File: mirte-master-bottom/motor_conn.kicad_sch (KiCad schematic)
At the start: 7 parts, among them U6 PCA9685PW

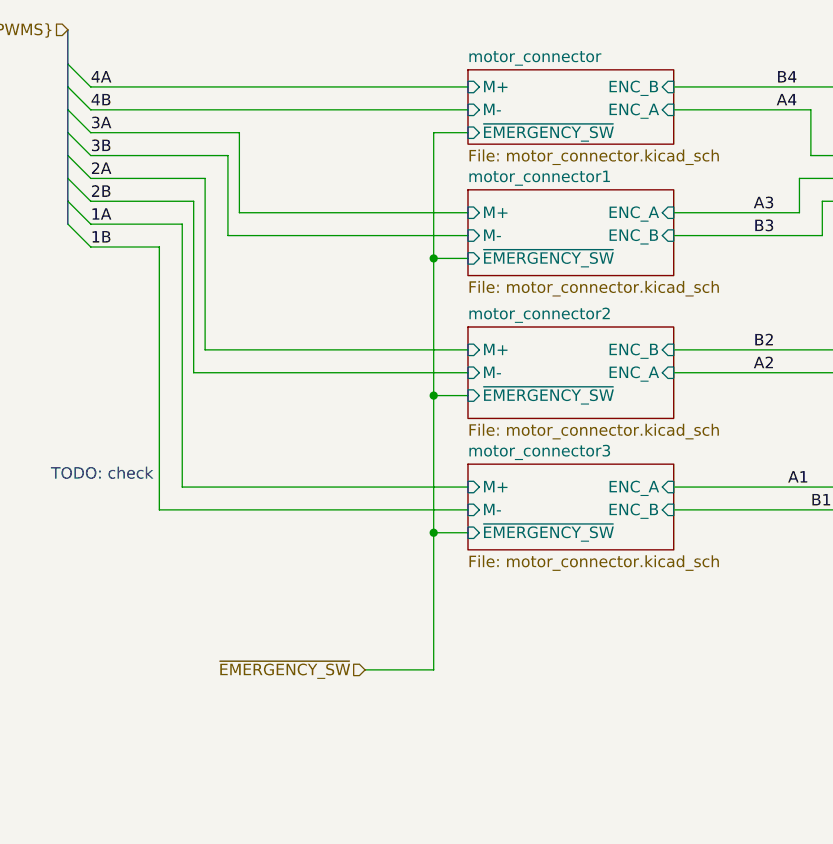
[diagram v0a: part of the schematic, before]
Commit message: Cleanups, text fixes for 3rd test pcb with assembly
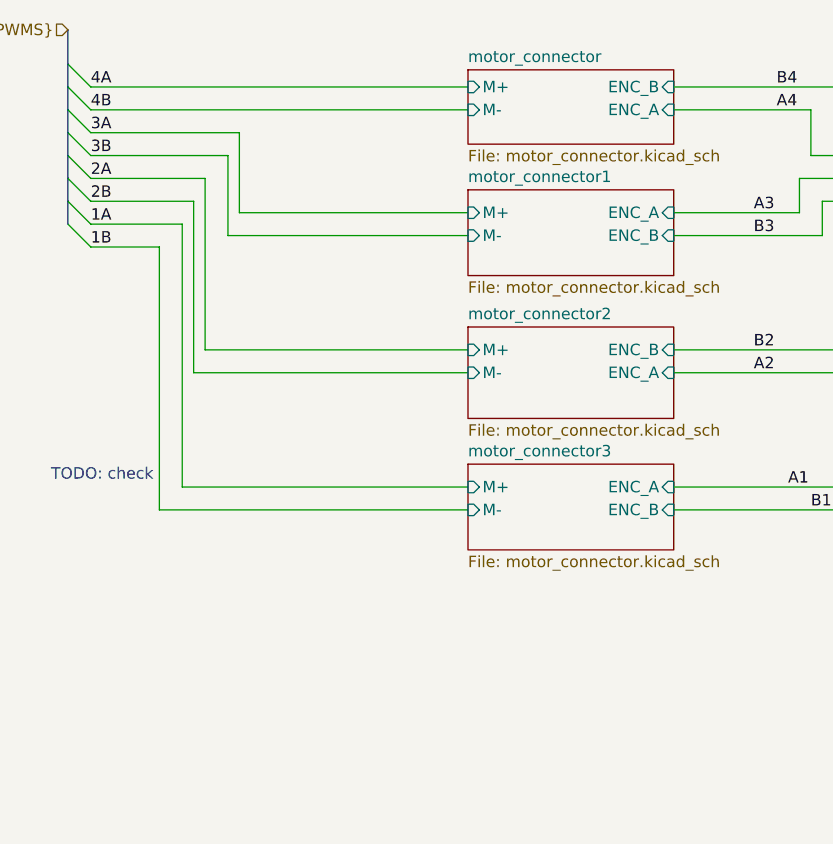
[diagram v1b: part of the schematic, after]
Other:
- sheet motor_connector ports: added none; removed ~{EMERGENCY_SW}
- sheet motor_connector1 ports: added none; removed ~{EMERGENCY_SW}
- sheet motor_connector2 ports: added none; removed ~{EMERGENCY_SW}
- sheet motor_connector3 ports: added none; removed ~{EMERGENCY_SW}
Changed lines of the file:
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@@
-	)
-	(junction
-		(at 149.86 105.41)
-		(diameter 0)
-		(color 0 0 0 0)
-	)
-	(junction
-		(at 149.86 90.17)
-		(diameter 0)
-		(color 0 0 0 0)
 	)
 	(junction
@@
 	)
 	(junction
-		(at 149.86 74.93)
-		(diameter 0)
-		(color 0 0 0 0)
-	)
-	(junction
 		(at 50.8 161.29)
 		(diameter 0)
@@
 	(wire
 		(pts
-			(xy 149.86 105.41) (xy 149.86 120.65)
-		)
-		(stroke
-			(width 0)
-			(type default)
-			(color 255 0 0 1)
-		)
-	)
-	(wire
-		(pts
 			(xy 111.76 60.96) (xy 128.27 60.96)
 		)
@@
 	(wire
 		(pts
-			(xy 149.86 60.96) (xy 149.86 74.93)
-		)
-		(stroke
-			(width 0)
-			(type default)
-			(color 255 0 0 1)
-		)
-	)
-	(wire
-		(pts
 			(xy 176.53 58.42) (xy 191.77 58.42)
 		)
@@
 	(wire
 		(pts
-			(xy 149.86 105.41) (xy 153.67 105.41)
-		)
-		(stroke
-			(width 0)
-			(type default)
-			(color 255 0 0 1)
-		)
-	)
-	(wire
-		(pts
 			(xy 196.85 60.96) (xy 208.28 60.96)
 		)
@@
 		)
 	)
-	(wire
-		(pts
-			(xy 142.24 120.65) (xy 149.86 120.65)
-		)
-		(stroke
-			(width 0)
-			(type default)
-			(color 255 0 0 1)
-		)
-	)
 	(bus
 		(pts
@@
 	(wire
 		(pts
-			(xy 149.86 74.93) (xy 149.86 90.17)
-		)
-		(stroke
-			(width 0)
-			(type default)
-			(color 255 0 0 1)
-		)
-	)
-	(wire
-		(pts
 			(xy 208.28 78.74) (xy 201.93 78.74)
 		)
@@
 	(wire
 		(pts
-			(xy 149.86 90.17) (xy 149.86 105.41)
-		)
-		(stroke
-			(width 0)
-			(type default)
-			(color 255 0 0 1)
-		)
-	)
-	(wire
-		(pts
-			(xy 149.86 90.17) (xy 153.67 90.17)
-		)
-		(stroke
-			(width 0)
-			(type default)
-			(color 255 0 0 1)
-		)
-	)
-	(wire
-		(pts
 			(xy 48.26 161.29) (xy 50.8 161.29)
 		)
@@
 	(wire
 		(pts
-			(xy 153.67 60.96) (xy 149.86 60.96)
-		)
-		(stroke
-			(width 0)
-			(type default)
-			(color 255 0 0 1)
-		)
-	)
-	(wire
-		(pts
 			(xy 194.31 85.09) (xy 194.31 71.12)
 		)
@@
 			(width 0)
 			(type default)
-		)
-	)
-	(wire
-		(pts
-			(xy 149.86 74.93) (xy 153.67 74.93)
-		)
-		(stroke
-			(width 0)
-			(type default)
-			(color 255 0 0 1)
 		)
 	)
@@
 		(shape input)
 		(at 109.22 49.53 180)
-		(effects
-			(font
-				(size 1.27 1.27)
-			)
-			(justify right)
-		)
-	)
-	(hierarchical_label "~{EMERGENCY_SW}"
-		(shape input)
-		(at 142.24 120.65 180)
 		(effects
 			(font
@@
 			)
 		)
-		(pin "~{EMERGENCY_SW}" input
-			(at 153.67 105.41 180)
-			(effects
-				(font
-					(size 1.27 1.27)
-				)
-				(justify left)
-			)
-		)
 		(instances
 			(project "mirte-master"
@@
 			)
 		)
-		(pin "~{EMERGENCY_SW}" input
-			(at 153.67 60.96 180)
-			(effects
-				(font
-					(size 1.27 1.27)
-				)
-				(justify left)
-			)
-		)
 		(instances
 			(project "mirte-master"
@@
 			)
 		)
-		(pin "~{EMERGENCY_SW}" input
-			(at 153.67 74.93 180)
-			(effects
-				(font
-					(size 1.27 1.27)
-				)
-				(justify left)
-			)
-		)
 		(instances
 			(project "mirte-master"
@@
 			)
 		)
-		(pin "~{EMERGENCY_SW}" input
-			(at 153.67 90.17 180)
-			(effects
-				(font
-					(size 1.27 1.27)
-				)
-				(justify left)
-			)
-		)

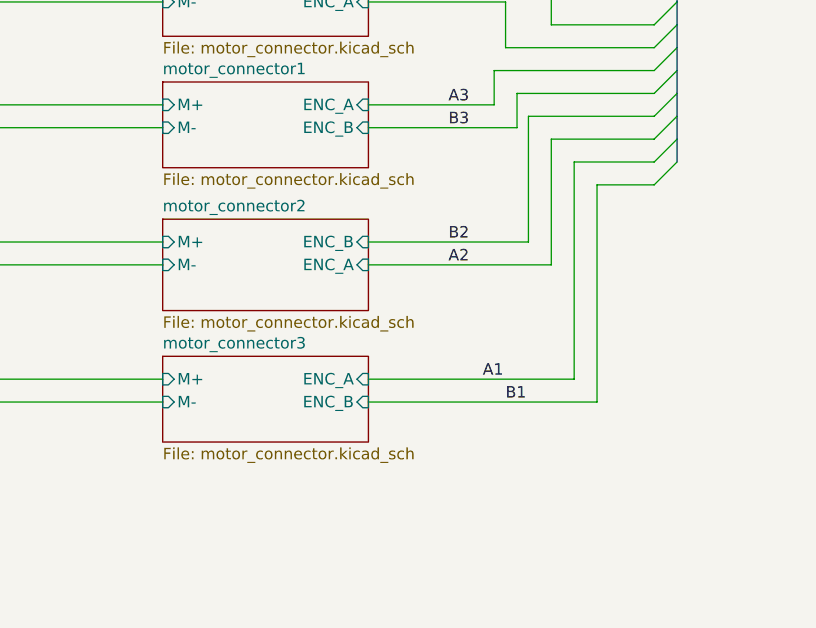
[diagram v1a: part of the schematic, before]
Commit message: MM: motor leds same color, emergency button screw, start button led screw, drc exclusions
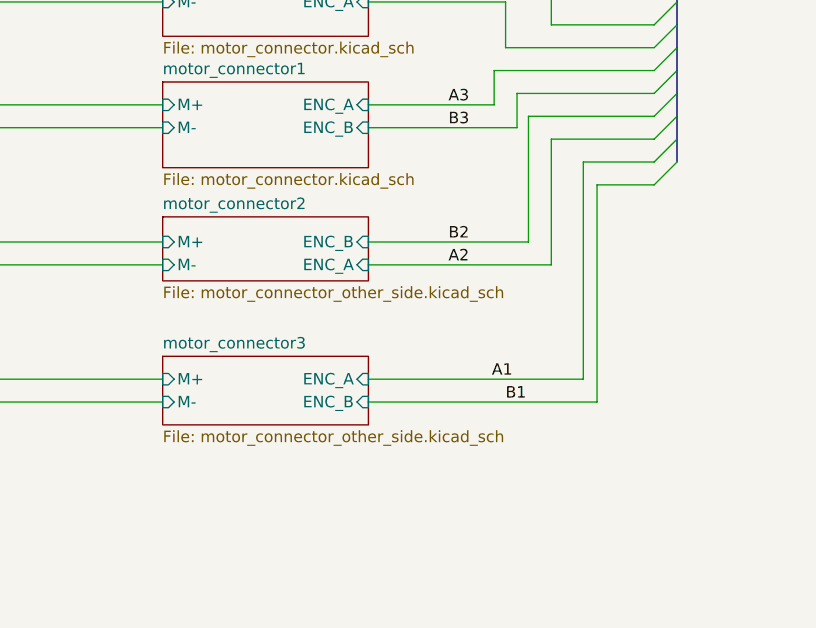
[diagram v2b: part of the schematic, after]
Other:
- sheet motor_connector2: file motor_connector.kicad_sch -> motor_connector_other_side.kicad_sch
- sheet motor_connector3: file motor_connector.kicad_sch -> motor_connector_other_side.kicad_sch
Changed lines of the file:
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@@
+	(wire
+		(pts
+			(xy 176.53 102.87) (xy 201.93 102.87)
+		)
+		(stroke
+			(width 0)
+			(type default)
+		)
+	)
 	(wire
 		(pts
@@
 	(wire
 		(pts
-			(xy 199.39 76.2) (xy 208.28 76.2)
+			(xy 200.406 76.2) (xy 208.28 76.2)
 		)
 		(stroke
@@
 	(wire
 		(pts
-			(xy 176.53 100.33) (xy 199.39 100.33)
+			(xy 176.53 100.33) (xy 200.406 100.33)
 		)
 		(stroke
@@
 	(wire
 		(pts
-			(xy 199.39 100.33) (xy 199.39 76.2)
+			(xy 200.406 100.33) (xy 200.406 76.2)
 		)
 		(stroke
@@
 		(pts
 			(xy 190.5 69.85) (xy 190.5 66.04)
-		)
-		(stroke
-			(width 0)
-			(type default)
-		)
-	)
-	(wire
-		(pts
-			(xy 201.93 102.87) (xy 176.53 102.87)
 		)
 		(stroke
@@
 	)
 	(label "A1"
-		(at 189.23 100.33 0)
+		(at 190.246 100.33 0)
 		(effects
 			(font
@@
 	(sheet
 		(at 153.67 97.79)
-		(size 22.86 9.525)
+		(size 22.86 7.62)
 		(exclude_from_sim no)
 		(in_bom yes)
@@
 			)
 		)
-		(property "Sheetfile" "motor_connector.kicad_sch"
-			(at 153.67 107.8996 0)
+		(property "Sheetfile" "motor_connector_other_side.kicad_sch"
+			(at 153.67 105.9946 0)
 			(effects
 				(font
@@
 	)
 	(sheet
-		(at 153.67 82.55)
-		(size 22.86 10.16)
+		(at 153.67 82.296)
+		(size 22.86 7.112)
 		(exclude_from_sim no)
 		(in_bom yes)
@@
 		)
 		(property "Sheetname" "motor_connector2"
-			(at 153.67 81.8384 0)
+			(at 153.67 81.5844 0)
 			(effects
 				(font
@@
 			)
 		)
-		(property "Sheetfile" "motor_connector.kicad_sch"
-			(at 153.67 93.2946 0)
-			(effects
-				(font
+		(property "Sheetfile" "motor_connector_other_side.kicad_sch"
+			(at 153.67 89.9926 0)
+			(effects
+				(font

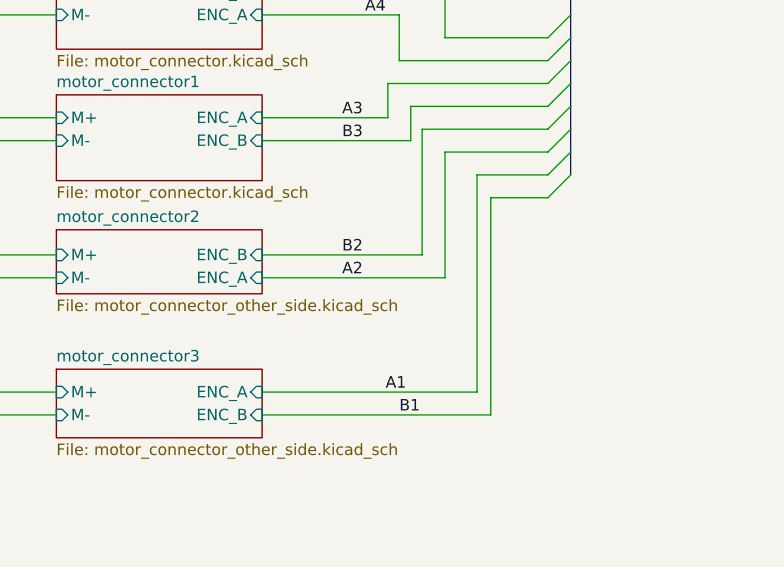
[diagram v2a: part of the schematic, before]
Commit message: MM: ERC&DRC fixes + change hbridge cap
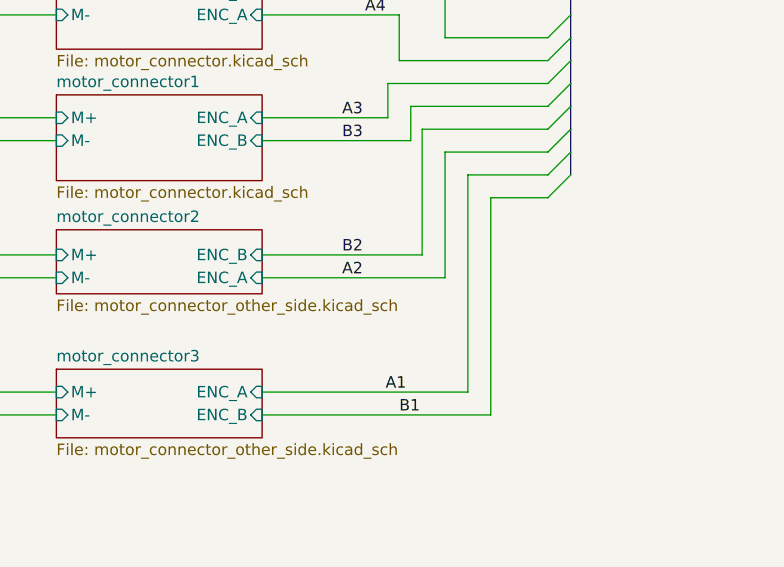
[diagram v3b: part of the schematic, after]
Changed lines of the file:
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@@
 	(wire
 		(pts
-			(xy 200.406 76.2) (xy 208.28 76.2)
+			(xy 199.39 76.2) (xy 208.28 76.2)
 		)
 		(stroke
@@
 	(wire
 		(pts
-			(xy 176.53 100.33) (xy 200.406 100.33)
+			(xy 176.53 100.33) (xy 199.39 100.33)
 		)
 		(stroke
@@
 	(wire
 		(pts
-			(xy 200.406 100.33) (xy 200.406 76.2)
-		)
-		(stroke
+			(xy 199.39 100.33) (xy 199.39 76.2)
+		)
+		(stroke

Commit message: MM: order big
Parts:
- R10, R11, R12, R13, R14, R9, U6: now left out of the parts list
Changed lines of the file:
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@@
 		(unit 1)
 		(exclude_from_sim no)
-		(in_bom yes)
+		(in_bom no)
 		(on_board no)
 		(dnp yes)
@@
 		(unit 1)
 		(exclude_from_sim no)
-		(in_bom yes)
+		(in_bom no)
 		(on_board no)
 		(dnp yes)
@@
 		(unit 1)
 		(exclude_from_sim no)
-		(in_bom yes)
+		(in_bom no)
 		(on_board no)
 		(dnp yes)
@@
 		(unit 1)
 		(exclude_from_sim no)
-		(in_bom yes)
+		(in_bom no)
 		(on_board no)
 		(dnp yes)
@@
 		(unit 1)
 		(exclude_from_sim no)
-		(in_bom yes)
+		(in_bom no)
 		(on_board no)
 		(dnp yes)
@@
 		(unit 1)
 		(exclude_from_sim no)
-		(in_bom yes)
+		(in_bom no)
 		(on_board no)
 		(dnp yes)
@@
 		(unit 1)
 		(exclude_from_sim no)
-		(in_bom yes)
-		(on_board no)
-		(dnp yes)
+		(in_bom no)
+		(on_board no)
+		(dnp yes)
